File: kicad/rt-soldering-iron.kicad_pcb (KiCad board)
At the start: 2 copper layers, 74.9 x 20.3 mm, 126 parts, among them J1 IRON_TIP, J2 BARREL_JACK, J3 CONN_01X04, Q1 SIA483DJ-T1-GE3, Q2 FDG6301N_F085, Q3 MMBT3904, Q4 MMBT3906WT1G, Q5 FDG6301N_F085, Q6 MMBT3906WT1G, Q7 FDG6301N_F085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

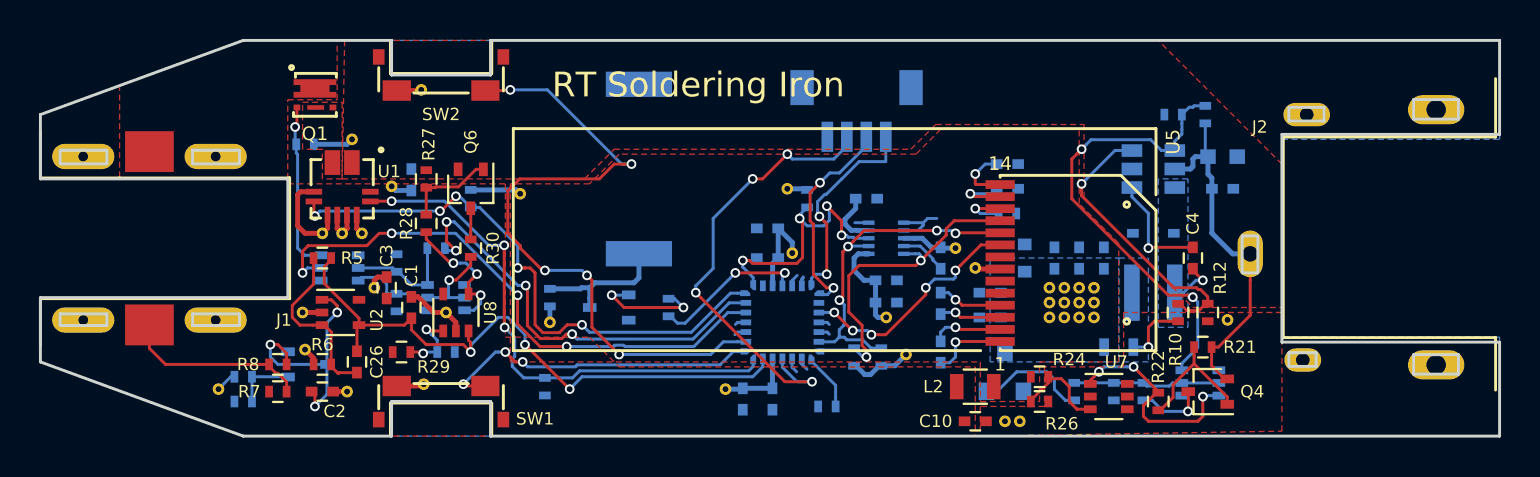
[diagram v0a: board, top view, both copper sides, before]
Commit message: Changed method for building oval pins for gerber export
When the gerbers need to be exported, the cutouts should be moved down
from the user drawing layer. The gerbers should be exported and the
board revered to the previous state. The gerbers will now be stored in
the git repository since I've learned it's dumb not to keep a copy of
those.
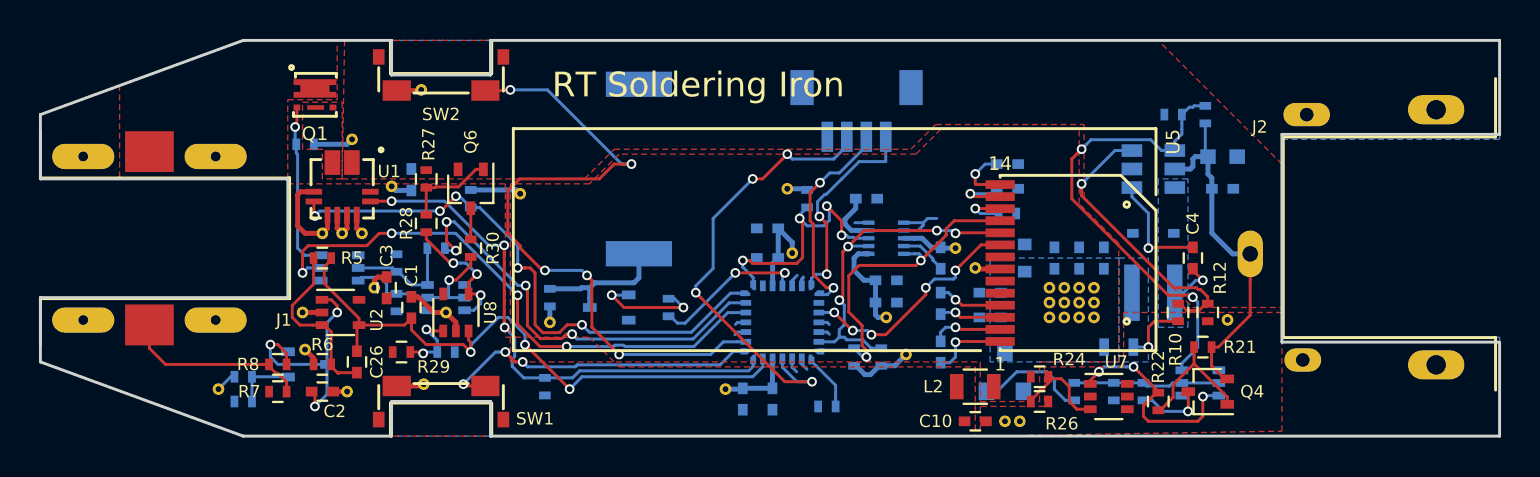
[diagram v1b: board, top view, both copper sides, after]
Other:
- outline, holes or cut-outs redrawn
- board text added: "Before sending gerbers, move edge cuts for the oval pins down from the Dwgs.User layer. Then move them back. Do not rebuild the copper pours."
- board text removed: "Before sending gerbers, add edge cuts for the oval pins. Do not rebuild the copper pours."
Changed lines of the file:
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@@
     (links 262)
     (no_connects 5)
-    (area 116.510999 86.284999 191.591001 106.755001)
+    (area 88.663824 67.629 223.75 109.560572)
     (thickness 1.6)
     (drawings 65)
@@
     (zone_45_only yes)
     (trace_min 0.1524)
-    (segment_width 0.2)
+    (segment_width 0.15)
     (edge_width 0.15)
     (via_size 0.5)
@@
     )
   )
-  (gr_line (start 187.1 103.5) (end 187.1 102.5) (layer Edge.Cuts) (width 0.15))
-  (gr_line (start 189.4 103.5) (end 187.1 103.5) (layer Edge.Cuts) (width 0.15))
-  (gr_line (start 189.4 102.5) (end 189.4 103.5) (layer Edge.Cuts) (width 0.15))
-  (gr_line (start 187.1 102.5) (end 189.4 102.5) (layer Edge.Cuts) (width 0.15))
-  (gr_line (start 187.1 90.4) (end 187.1 89.4) (layer Edge.Cuts) (width 0.15))
-  (gr_line (start 189.4 90.4) (end 187.1 90.4) (layer Edge.Cuts) (width 0.15))
-  (gr_line (start 189.4 89.4) (end 189.4 90.4) (layer Edge.Cuts) (width 0.15))
-  (gr_line (start 187.1 89.4) (end 189.4 89.4) (layer Edge.Cuts) (width 0.15))
-  (gr_line (start 180.7 103.1) (end 180.7 102.4) (layer Edge.Cuts) (width 0.15))
-  (gr_line (start 182.1 103.1) (end 180.7 103.1) (layer Edge.Cuts) (width 0.15))
-  (gr_line (start 182.1 102.4) (end 182.1 103.1) (layer Edge.Cuts) (width 0.15))
-  (gr_line (start 180.7 102.4) (end 182.1 102.4) (layer Edge.Cuts) (width 0.15))
-  (gr_line (start 180.7 90.5) (end 180.7 89.8) (layer Edge.Cuts) (width 0.15))
-  (gr_line (start 182.5 90.5) (end 180.7 90.5) (layer Edge.Cuts) (width 0.15))
-  (gr_line (start 182.5 89.8) (end 182.5 90.5) (layer Edge.Cuts) (width 0.15))
-  (gr_line (start 180.7 89.8) (end 182.5 89.8) (layer Edge.Cuts) (width 0.15))
-  (gr_line (start 178.3 98.3) (end 178.3 96.4) (layer Edge.Cuts) (width 0.15))
-  (gr_line (start 179.1 98.3) (end 178.3 98.3) (layer Edge.Cuts) (width 0.15))
-  (gr_line (start 179.1 96.4) (end 179.1 98.3) (layer Edge.Cuts) (width 0.15))
-  (gr_line (start 178.3 96.4) (end 179.1 96.4) (layer Edge.Cuts) (width 0.15))
-  (gr_line (start 117.6 101) (end 117.6 100.4) (layer Edge.Cuts) (width 0.15))
-  (gr_line (start 120 101) (end 117.6 101) (layer Edge.Cuts) (width 0.15))
-  (gr_line (start 120 100.4) (end 120 101) (layer Edge.Cuts) (width 0.15))
-  (gr_line (start 117.6 100.4) (end 120 100.4) (layer Edge.Cuts) (width 0.15))
-  (gr_line (start 124.4 101) (end 124.4 100.4) (layer Edge.Cuts) (width 0.15))
-  (gr_line (start 126.8 101) (end 124.4 101) (layer Edge.Cuts) (width 0.15))
-  (gr_line (start 126.8 100.4) (end 126.8 101) (layer Edge.Cuts) (width 0.15))
-  (gr_line (start 124.4 100.4) (end 126.8 100.4) (layer Edge.Cuts) (width 0.15))
-  (gr_line (start 124.4 92.7) (end 124.4 92) (layer Edge.Cuts) (width 0.15))
-  (gr_line (start 126.8 92.7) (end 124.4 92.7) (layer Edge.Cuts) (width 0.15))
-  (gr_line (start 126.8 92) (end 126.8 92.7) (layer Edge.Cuts) (width 0.15))
-  (gr_line (start 124.4 92) (end 126.8 92) (layer Edge.Cuts) (width 0.15))
-  (gr_line (start 117.6 92.7) (end 117.6 92) (layer Edge.Cuts) (width 0.15))
-  (gr_line (start 120 92.7) (end 117.6 92.7) (layer Edge.Cuts) (width 0.15))
-  (gr_line (start 120 92) (end 120 92.7) (layer Edge.Cuts) (width 0.15))
-  (gr_line (start 117.6 92) (end 120 92) (layer Edge.Cuts) (width 0.15))
+  (gr_line (start 187.1 103.5) (end 187.1 102.5) (layer Dwgs.User) (width 0.15))
+  (gr_line (start 189.4 103.5) (end 187.1 103.5) (layer Dwgs.User) (width 0.15))
+  (gr_line (start 189.4 102.5) (end 189.4 103.5) (layer Dwgs.User) (width 0.15))
+  (gr_line (start 187.1 102.5) (end 189.4 102.5) (layer Dwgs.User) (width 0.15))
+  (gr_line (start 187.1 90.4) (end 187.1 89.4) (layer Dwgs.User) (width 0.15))
+  (gr_line (start 189.4 90.4) (end 187.1 90.4) (layer Dwgs.User) (width 0.15))
+  (gr_line (start 189.4 89.4) (end 189.4 90.4) (layer Dwgs.User) (width 0.15))
+  (gr_line (start 187.1 89.4) (end 189.4 89.4) (layer Dwgs.User) (width 0.15))
+  (gr_line (start 180.7 103.1) (end 180.7 102.4) (layer Dwgs.User) (width 0.15))
+  (gr_line (start 182.1 103.1) (end 180.7 103.1) (layer Dwgs.User) (width 0.15))
+  (gr_line (start 182.1 102.4) (end 182.1 103.1) (layer Dwgs.User) (width 0.15))
+  (gr_line (start 180.7 102.4) (end 182.1 102.4) (layer Dwgs.User) (width 0.15))
+  (gr_line (start 180.7 90.5) (end 180.7 89.8) (layer Dwgs.User) (width 0.15))
+  (gr_line (start 182.5 90.5) (end 180.7 90.5) (layer Dwgs.User) (width 0.15))
+  (gr_line (start 182.5 89.8) (end 182.5 90.5) (layer Dwgs.User) (width 0.15))
+  (gr_line (start 180.7 89.8) (end 182.5 89.8) (layer Dwgs.User) (width 0.15))
+  (gr_line (start 178.3 98.3) (end 178.3 96.4) (layer Dwgs.User) (width 0.15))
+  (gr_line (start 179.1 98.3) (end 178.3 98.3) (layer Dwgs.User) (width 0.15))
+  (gr_line (start 179.1 96.4) (end 179.1 98.3) (layer Dwgs.User) (width 0.15))
+  (gr_line (start 178.3 96.4) (end 179.1 96.4) (layer Dwgs.User) (width 0.15))
+  (gr_line (start 117.6 101) (end 117.6 100.4) (layer Dwgs.User) (width 0.15))
+  (gr_line (start 120 101) (end 117.6 101) (layer Dwgs.User) (width 0.15))
+  (gr_line (start 120 100.4) (end 120 101) (layer Dwgs.User) (width 0.15))
+  (gr_line (start 117.6 100.4) (end 120 100.4) (layer Dwgs.User) (width 0.15))
+  (gr_line (start 124.4 101) (end 124.4 100.4) (layer Dwgs.User) (width 0.15))
+  (gr_line (start 126.8 101) (end 124.4 101) (layer Dwgs.User) (width 0.15))
+  (gr_line (start 126.8 100.4) (end 126.8 101) (layer Dwgs.User) (width 0.15))
+  (gr_line (start 124.4 100.4) (end 126.8 100.4) (layer Dwgs.User) (width 0.15))
+  (gr_line (start 124.4 92.7) (end 124.4 92) (layer Dwgs.User) (width 0.15))
+  (gr_line (start 126.8 92.7) (end 124.4 92.7) (layer Dwgs.User) (width 0.15))
+  (gr_line (start 126.8 92) (end 126.8 92.7) (layer Dwgs.User) (width 0.15))
+  (gr_line (start 124.4 92) (end 126.8 92) (layer Dwgs.User) (width 0.15))
+  (gr_line (start 117.6 92.7) (end 117.6 92) (layer Dwgs.User) (width 0.15))
+  (gr_line (start 120 92.7) (end 117.6 92.7) (layer Dwgs.User) (width 0.15))
+  (gr_line (start 120 92) (end 120 92.7) (layer Dwgs.User) (width 0.15))
+  (gr_line (start 117.6 92) (end 120 92) (layer Dwgs.User) (width 0.15))
   (gr_line (start 134.62 86.36) (end 127 86.36) (layer Edge.Cuts) (width 0.15))
   (gr_line (start 134.62 88.138) (end 134.62 86.36) (layer Edge.Cuts) (width 0.15))
@@
   (gr_line (start 139.7 104.902) (end 134.62 104.902) (layer Edge.Cuts) (width 0.15))
   (gr_line (start 139.7 106.68) (end 139.7 104.902) (layer Edge.Cuts) (width 0.15))
-  (gr_text "Before sending gerbers, add edge cuts for the oval pins.\nDo not rebuild the copper pours." (at 147.828 70.104) (layer Cmts.User)
+  (gr_text "Before sending gerbers, move edge cuts for the oval pins\ndown from the Dwgs.User layer. Then move them back.\nDo not rebuild the copper pours." (at 147.828 70.104) (layer Cmts.User)
     (effects (font (size 1.5 1.5) (thickness 0.3)))
   )
